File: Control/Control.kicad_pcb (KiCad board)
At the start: 2 copper layers, 89 parts, among them J1 Conn_02x08_Odd_Even, J2 Conn_02x08_Odd_Even, J3 Conn_02x15_Odd_Even, U1 74AHC1G04, U2 74HC73, U3 74LS161, U4 SST39SF020, U5 SST39SF020, U6 SST39SF020, U7 SST39SF020, U8 SN74AHCT16374DGGR, U9 74AHC1G08

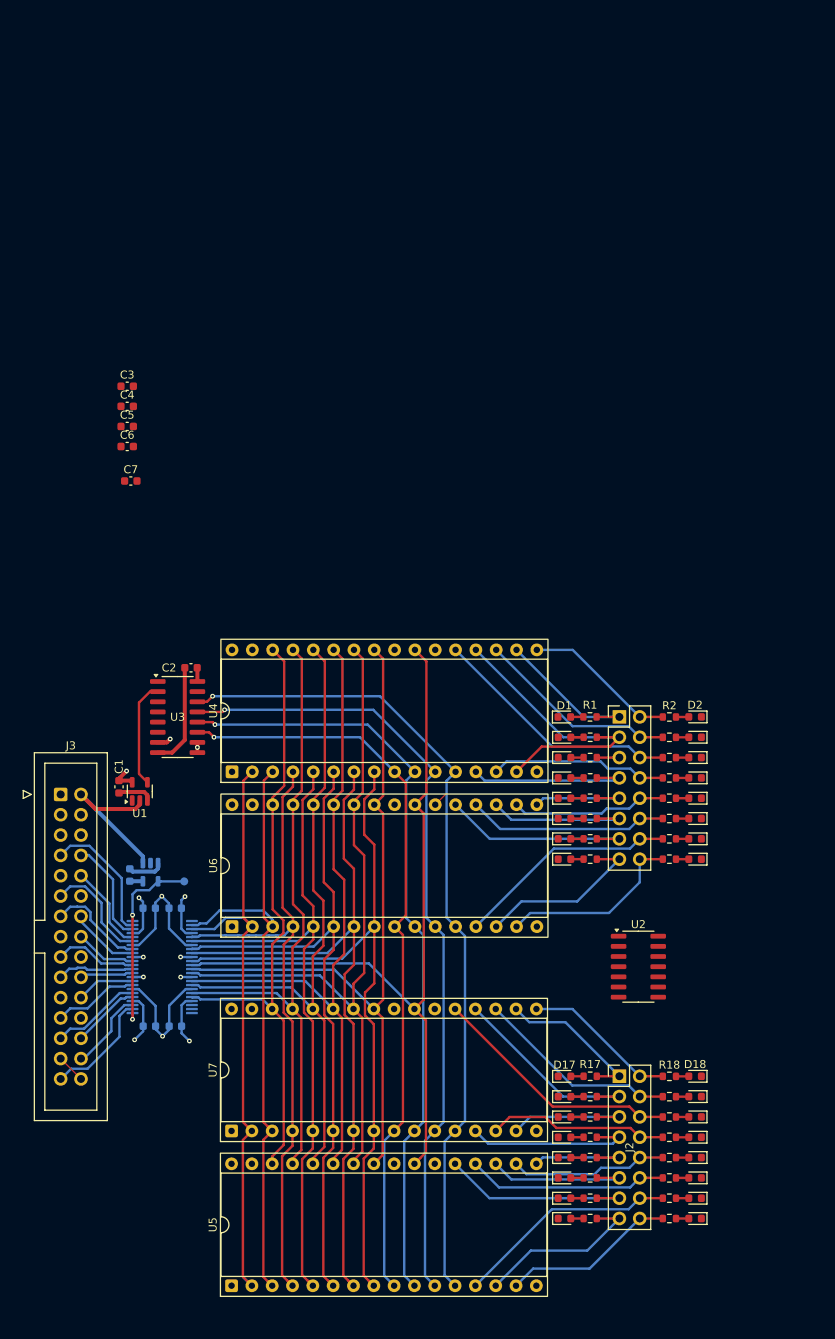
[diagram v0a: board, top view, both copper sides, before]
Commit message: Cleanup, added photos and README overhaul
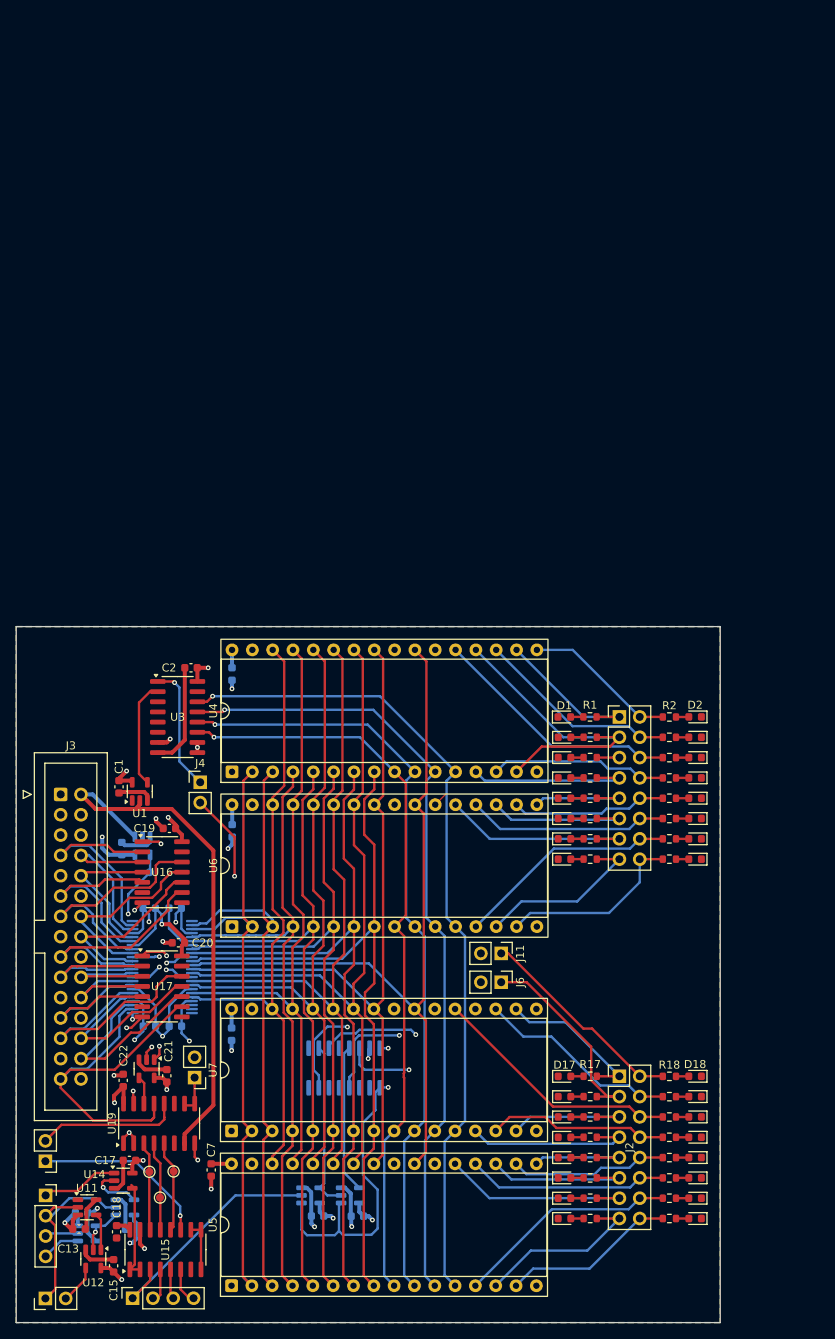
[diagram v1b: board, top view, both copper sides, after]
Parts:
- removed C3: 0.1uF, Capacitor_SMD:C_0603_1608Metric
- removed U2: 74HC73, Package_SO:SOIC-14_3.9x8.7mm_P1.27mm
- added C13: 0.1uF, Capacitor_SMD:C_0603_1608Metric, F.Cu at (21.9, 168.3)
- added C14: 0.1uF, Capacitor_SMD:C_0603_1608Metric, B.Cu at (22.2, 166.2)
- added C15: 0.1uF, Capacitor_SMD:C_0603_1608Metric, F.Cu at (26.2, 172.9)
- added C16: 0.1uF, Capacitor_SMD:C_0603_1608Metric, B.Cu at (28.4, 168.3)
- added C17: 0.1uF, Capacitor_SMD:C_0603_1608Metric, F.Cu at (28.1, 159.7)
- added C18: 0.1uF, Capacitor_SMD:C_0603_1608Metric, F.Cu at (26.6, 168.7)
- added C19: 0.1uF, Capacitor_SMD:C_0603_1608Metric, F.Cu at (33.1, 118.2)
- added C20: 0.1uF, Capacitor_SMD:C_0603_1608Metric, F.Cu at (34.3, 132.5)
- added C21: 0.1uF, Capacitor_SMD:C_0603_1608Metric, F.Cu at (32.8, 149.2)
- added C22: 0.1uF, Capacitor_SMD:C_0603_1608Metric, F.Cu at (27.4, 149.7)
- added C23: 0.1uF, Capacitor_SMD:C_0603_1608Metric, B.Cu at (51.7, 166.7)
- added C24: 0.1uF, Capacitor_SMD:C_0603_1608Metric, B.Cu at (56.6, 166.7)
- added J10: Conn_01x02, Connector_PinHeader_2.54mm:PinHeader_1x02_P2.54mm_Vertical, F.Cu at (36.3, 149.4)
- added J11: Conn_01x02, Connector_PinHeader_2.54mm:PinHeader_1x02_P2.54mm_Vertical, F.Cu at (74.6, 133.8)
- added J4: MCR-MCRI, Connector_PinHeader_2.54mm:PinHeader_1x02_P2.54mm_Vertical, F.Cu at (37.0, 112.5)
- added J5: Conn_01x04, Connector_PinSocket_2.54mm:PinSocket_1x04_P2.54mm_Vertical, F.Cu at (17.7, 164.1)
- added J6: Conn_01x02, Connector_PinHeader_2.54mm:PinHeader_1x02_P2.54mm_Vertical, F.Cu at (74.6, 137.4)
- added J7: Conn_01x02, Connector_PinHeader_2.54mm:PinHeader_1x02_P2.54mm_Vertical, F.Cu at (17.6, 177.0)
- added J8: Conn_01x04, Connector_PinSocket_2.54mm:PinSocket_1x04_P2.54mm_Vertical, F.Cu at (28.6, 176.9)
- added J9: Conn_01x02, Connector_PinHeader_2.54mm:PinHeader_1x02_P2.54mm_Vertical, F.Cu at (17.6, 159.8)
- added TP2: TestPoint, TestPoint:TestPoint_Pad_D1.0mm, F.Cu at (30.6, 161.2)
- added TP3: TestPoint, TestPoint:TestPoint_Pad_D1.0mm, F.Cu at (32.0, 164.4)
- added TP4: TestPoint, TestPoint:TestPoint_Pad_D1.0mm, F.Cu at (33.7, 161.1)
- added U10: 74AHC1G08, Package_TO_SOT_SMD:SOT-23-5, B.Cu at (22.8, 168.8)
- added U11: 74AHC1G04, Package_TO_SOT_SMD:SOT-23-5, F.Cu at (22.9, 165.6)
- added U12: 74AHC1G32, Package_TO_SOT_SMD:SOT-23-5, F.Cu at (23.6, 172.0)
- added U13: 74AHC1G00, Package_TO_SOT_SMD:SOT-23-5, B.Cu at (27.6, 165.6)
- added U14: 74AHC1G32, Package_TO_SOT_SMD:SOT-23-5, F.Cu at (27.4, 162.3)
- added U15: 74HC173, Package_SO:SOIC-16_3.9x9.9mm_P1.27mm, F.Cu at (32.7, 170.9)
- added U16: 4078, Package_SO:SOIC-14_3.9x8.7mm_P1.27mm, F.Cu at (32.2, 123.7)
- added U17: 4078, Package_SO:SOIC-14_3.9x8.7mm_P1.27mm, F.Cu at (32.2, 138.0)
- added U18: 74AHC1G32, Package_TO_SOT_SMD:SOT-23-5, F.Cu at (30.3, 148.3)
- added U19: 74HC173, Package_SO:SOIC-16_3.9x9.9mm_P1.27mm, F.Cu at (31.9, 155.1)
- added U20: 74AHC1G08, Package_TO_SOT_SMD:SOT-23-5, B.Cu at (50.8, 164.1)
- added U21: 74AHC1G08, Package_TO_SOT_SMD:SOT-23-5, B.Cu at (55.8, 164.1)
- added U22: 74LS157, Package_SO:SOIC-16_3.9x9.9mm_P1.27mm, B.Cu at (55.0, 148.2)
- C4, C5, C6: moved to B.Cu
- moved C7 86.7 mm to (38.4, 160.9), turned to -90 degrees
- moved C6 74.6 mm to (40.9, 143.9), turned to -90 degrees
- moved C4 54.7 mm to (41.0, 118.5), turned to -90 degrees
- moved C5 33.6 mm to (41.0, 98.9), turned to -90 degrees
- moved TP1 4.45 mm to (30.7, 123.7)
- moved C12 3.45 mm to (27.2, 120.8)
- moved U9 3.45 mm to (29.8, 120.4)
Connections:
- net /bus_conn/IO0 renamed /ALU interface/BUS0
- net /bus_conn/IO1 renamed /ALU interface/BUS1
- net /bus_conn/IO10 renamed /ALU interface/BUS10
- net /bus_conn/IO11 renamed /ALU interface/BUS11
- net /bus_conn/IO12 renamed /ALU interface/BUS12
- net /bus_conn/IO13 renamed /ALU interface/BUS13
- net /bus_conn/IO14 renamed /ALU interface/BUS14
- net /bus_conn/IO15 renamed /ALU interface/BUS15
- net /bus_conn/IO2 renamed /ALU interface/BUS2
- net /bus_conn/IO3 renamed /ALU interface/BUS3
- net /bus_conn/IO4 renamed /ALU interface/BUS4
- net /bus_conn/IO5 renamed /ALU interface/BUS5
- net /bus_conn/IO6 renamed /ALU interface/BUS6
- net /bus_conn/IO7 renamed /ALU interface/BUS7
- net /bus_conn/IO8 renamed /ALU interface/BUS8
- net /bus_conn/IO9 renamed /ALU interface/BUS9
- U3 pad 1: unconnected-(U3-~{MR}-Pad1) -> Net-(J4-Pin_1)
- U7 pad 17: /PCE -> /PCEi
- U7 pad 20: /~{PCL} -> /~{PCL}i
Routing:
- net GND: track 57.1 -> 133.8 mm, vias 8 -> 25
- net +5V: track 41.9 -> 101.7 mm, vias 5 -> 17
- net /JNZ: track 22.7 -> 76.8 mm, vias 0 -> 1
- net /~{MCR}: track 31.6 -> 81.0 mm, vias 0 -> 1
- net /CLK: track 20.6 -> 68.0 mm
- net /~{ALO}: track 19.2 -> 62.6 mm
- net /ALU interface/BUS15: track 14.5 -> 49.8 mm
- net /jump logic/PCE: track 0.00 -> 34.4 mm, vias 0 -> 1
- net /FLG_ZERO: track 0.00 -> 30.5 mm
- net Net-(U16-Pad1): track 0.00 -> 30.2 mm, vias 0 -> 2
- net /PCEi: track 0.00 -> 27.6 mm, vias 0 -> 1
- net /register interface/R2: track 0.00 -> 26.1 mm
- net /jump logic/~{PCL}: track 0.00 -> 25.5 mm, vias 0 -> 1
- net /register interface/FLG_GPU_READY: track 0.00 -> 22.2 mm, vias 0 -> 1
- net /~{PCL}i: track 0.00 -> 21.0 mm, vias 0 -> 1
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- added copper zone on In2.Cu, net +5V
- added copper zone on B.Cu, net GND
- added copper zone on F.Cu, net GND
- added copper zone on In1.Cu, net GND
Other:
- board outline added: 88 x 87 mm
- copper layers 2 -> 4

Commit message: Finalized Control unit for fabrication
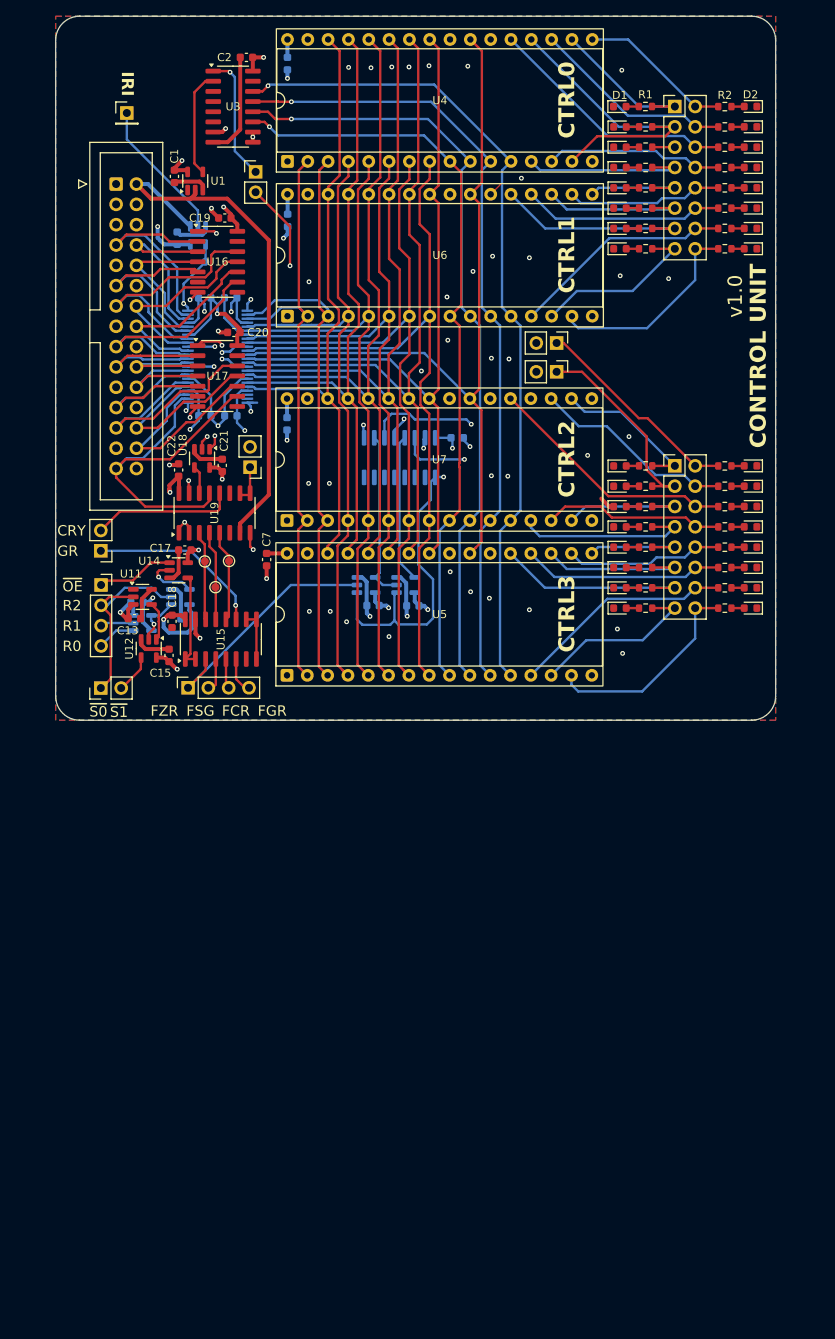
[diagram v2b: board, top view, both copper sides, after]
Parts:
- added C3: 0.1uF, Capacitor_SMD:C_0603_1608Metric, B.Cu at (69.1, 69.4)
- added J12: Conn_01x01, Connector_PinHeader_2.54mm:PinHeader_1x01_P2.54mm_Vertical, F.Cu at (27.8, 28.8)
- moved C1 76.6 mm to (33.8, 36.7)
- moved C13 76.6 mm to (28.8, 92.0)
- moved C15 76.6 mm to (33.1, 96.6)
- moved C18 76.6 mm to (33.5, 92.3)
- moved C2 76.6 mm to (42.8, 21.9)
- moved C20 76.6 mm to (41.2, 56.2)
- moved C21 76.6 mm to (39.8, 72.8)
- moved C23 76.6 mm to (58.6, 90.4)
- moved C4 76.6 mm to (47.9, 42.2)
- moved C7 76.6 mm to (45.3, 84.6)
- moved D10 76.6 mm to (105.8, 38.1)
- moved D11 76.6 mm to (89.5, 40.7)
- moved D13 76.6 mm to (89.5, 43.2)
- moved D14 76.6 mm to (105.8, 43.2)
- moved D18 76.6 mm to (105.8, 72.9)
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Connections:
- U22 pad 12: unconnected-(U22-Zd-Pad12) -> /jump logic/PCE
- U22 pad 4: /jump logic/~{PCL} -> unconnected-(U22-Za-Pad4)
- U22 pad 7: /jump logic/PCE -> unconnected-(U22-Zb-Pad7)
- U22 pad 9: unconnected-(U22-Zc-Pad9) -> /jump logic/~{PCL}
- U8 pad 1: /reg16/~{OE} -> GND
- U8 pad 24: /reg16/~{OE} -> GND
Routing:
- net /reg16/WE: track 0.00 -> 17.8 mm
- net /jump logic/PCE: track 34.4 -> 25.7 mm
- net +5V: track 101.7 -> 109.2 mm
- net GND: track 133.8 -> 139.8 mm, vias 25 -> 63
- net /D7: track 21.8 -> 26.4 mm
- net /jump logic/~{PCL}: track 25.5 -> 28.2 mm
- net /reg16/DOUT1: track 79.5 -> 77.2 mm
- net /ALF3: track 23.5 -> 25.7 mm
- net Net-(U8-1CLK): track 22.7 -> 24.4 mm
- net /~{PCL}i: track 21.0 -> 22.6 mm
- net /ALU interface/BUS15: track 49.8 -> 48.9 mm
- net /SWP: track 21.8 -> 22.6 mm
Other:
- board size 88 x 87 mm -> 90 x 88 mm
- board text added: "CONTROL UNIT"
- board text added: "CRY"
- board text added: "CTRL0"
- board text added: "CTRL1"
- board text added: "CTRL2"
- board text added: "CTRL3"
- board text added: "FCR"
- board text added: "FGR"
- board text added: "FSG"
- board text added: "FZR"
- board text added: "GR"
- board text added: "IRI"
- board text added: "R0"
- board text added: "R1"
- board text added: "R2"
- board text added: "v1.0"
- board text added: "~{OE}"
- board text added: "~{S0}"
- board text added: "~{S1}"

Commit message: Updated control unit and finalized for fabrication
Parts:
- added TP5: TestPoint, TestPoint:TestPoint_Pad_D1.0mm, B.Cu at (54.7, 26.4)
- added TP6: TestPoint, TestPoint:TestPoint_Pad_D1.0mm, B.Cu at (55.4, 32.9)
- added TP7: TestPoint, TestPoint:TestPoint_Pad_D1.0mm, B.Cu at (55.8, 28.6)
- added TP8: TestPoint, TestPoint:TestPoint_Pad_D1.0mm, B.Cu at (57.5, 30.8)
- moved C15 5.57 mm to (38.5, 97.8)
- moved C17 5.57 mm to (40.5, 84.6)
- moved C18 5.57 mm to (38.9, 93.6)
- moved TP2 5.57 mm to (43.0, 86.1)
- moved TP4 5.57 mm to (46.0, 86.0)
- moved U10 5.57 mm to (35.2, 93.8)
- moved U13 5.57 mm to (40.0, 90.5)
- moved U18 5.57 mm to (42.7, 73.2)
- moved U20 5.57 mm to (63.2, 89.0)
- moved U21 5.57 mm to (68.1, 89.0)
- moved C19 5.57 mm to (45.5, 43.1)
- moved C20 5.57 mm to (46.6, 57.4)
- moved J12 5.57 mm to (33.3, 30.0)
- moved U16 5.57 mm to (44.6, 48.6)
- moved U3 5.57 mm to (46.5, 29.2)
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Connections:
- net /register interface/FLG_CARRY renamed Net-(J8-Pin_3)
- net /register interface/FLG_SIGN renamed Net-(J8-Pin_2)
- U15 pad 7: /register interface/CLK -> /CLK
- U4 pad 24: unconnected-(U4-OE-Pad24) -> GND
- U4 pad 31: unconnected-(U4-PGM-Pad31) -> +5V
- U5 pad 24: unconnected-(U5-OE-Pad24) -> GND
- U5 pad 31: unconnected-(U5-PGM-Pad31) -> +5V
- U6 pad 24: unconnected-(U6-OE-Pad24) -> GND
- U6 pad 31: unconnected-(U6-PGM-Pad31) -> +5V
- U7 pad 24: unconnected-(U7-OE-Pad24) -> GND
- U7 pad 31: unconnected-(U7-PGM-Pad31) -> +5V
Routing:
- net /ALU interface/BUS15: track 48.9 -> 51.9 mm
- net /ALU interface/BUS4: track 31.9 -> 34.6 mm
- net /ALU interface/BUS14: track 26.5 -> 29.1 mm
- net /ALU interface/BUS11: track 22.3 -> 25.0 mm
- net /ALU interface/BUS13: track 24.2 -> 26.8 mm
- net /ALU interface/BUS10: track 15.5 -> 18.1 mm
- net /ALU interface/BUS9: track 14.8 -> 17.4 mm
- net /CLK: track 68.0 -> 70.5 mm
- net /ALU interface/BUS2: track 18.9 -> 21.4 mm
- net /ALU interface/BUS3: track 25.7 -> 28.1 mm
- net /ALU interface/BUS8: track 21.1 -> 23.0 mm
- net /ALU interface/BUS5: track 24.4 -> 26.3 mm
- net /ALU interface/BUS12: track 31.2 -> 33.0 mm
- net /ALU interface/BUS7: track 30.8 -> 32.6 mm
- net /ALU interface/BUS6: track 24.2 -> 26.0 mm
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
